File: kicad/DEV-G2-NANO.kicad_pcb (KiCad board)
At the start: 6 copper layers, 76.2 x 20.3 mm, 59 parts, among them J2 Lower Bank, J3 USB C, J3 Upper Bank, J4 HIC SWD, J5 RTC Battery, SW1 PTS815, U1 MIMXRT1171DVMAB, U10 TPS62825, U2 MAYA-W166-00B, U3 LSM6DSV, U4 LIS2MDL, U5 RTMC-G2-4IQ48, U6 W25Q64JWUUIQ, U7 MKL26Z128VFM4, U8 LM66200, U9 TPS62086, Y1 8MHz, Y2 16MHz, Y3 24MHz, Y4 32.768kHz

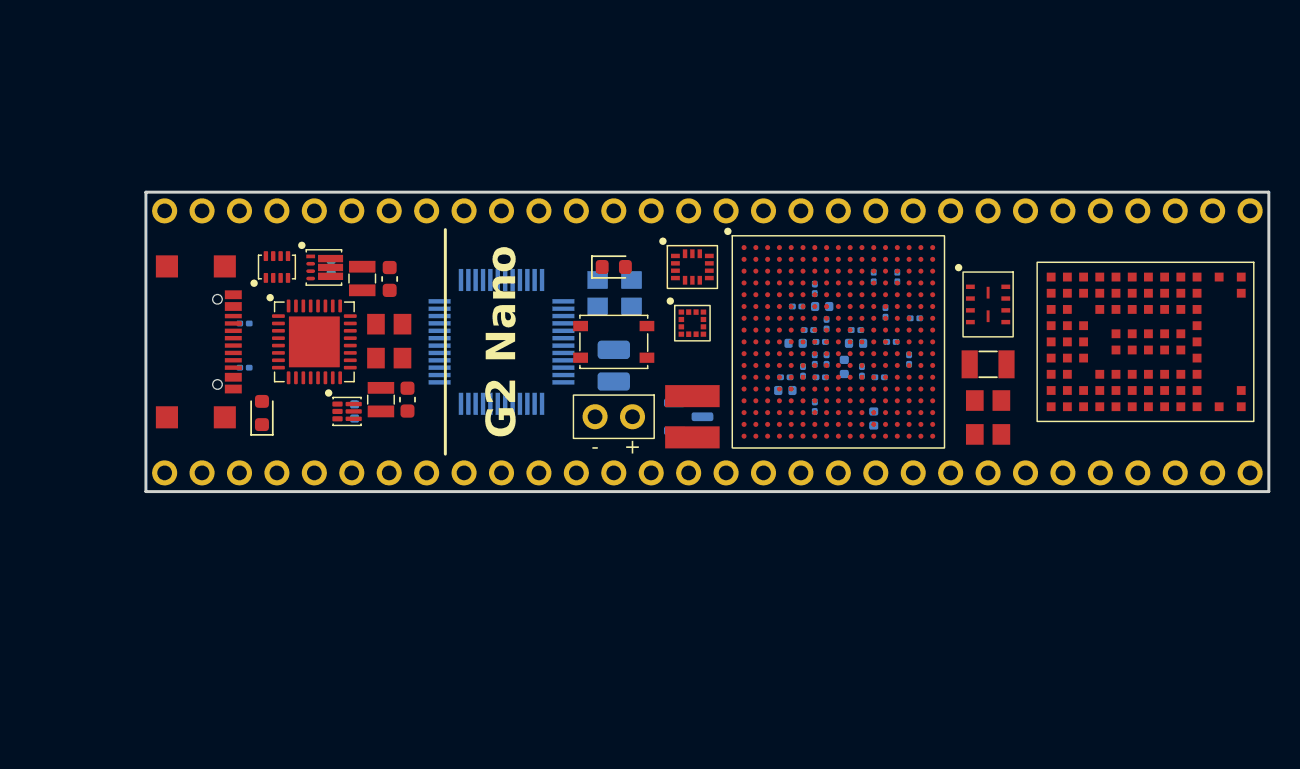
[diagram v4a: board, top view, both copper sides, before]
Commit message: finished preliminary routing
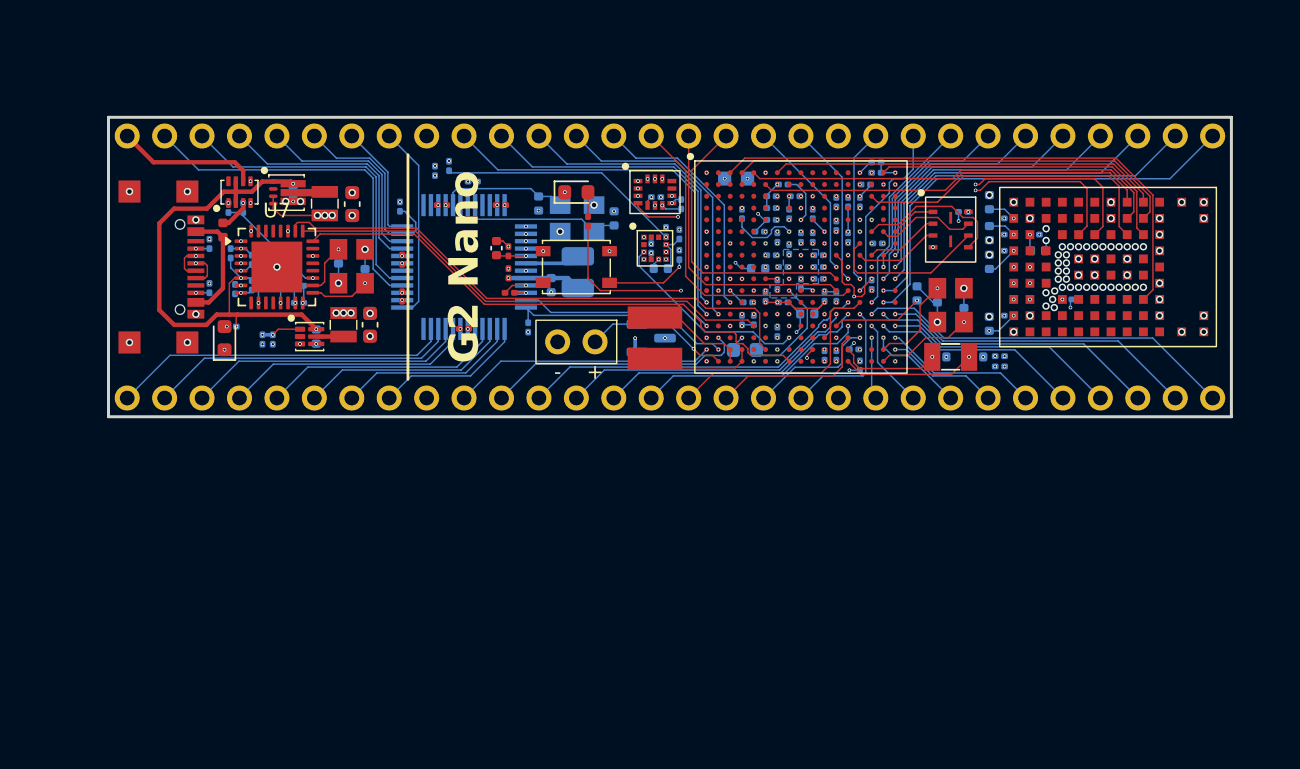
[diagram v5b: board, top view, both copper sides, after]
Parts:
- removed the C44 at (159.0, 98.5)
- removed the C47 at (166.2, 95.2)
- removed the C49 at (161.5, 92.8)
- removed the C50 at (165.4, 97.7)
- removed the C68 at (163.0, 97.0)
- removed the J3 at (190.5, 86.4)
- added C1: 100nF, Capacitor_SMD:C_0201_0603Metric, B.Cu at (174.1, 89.1)
- added C10: 10μF, Capacitor_SMD:C_0402_1005Metric, B.Cu at (172.8, 87.9)
- added C11: 100nF, Capacitor_SMD:C_0201_0603Metric, B.Cu at (151.9, 85.9)
- added C12: 100nF, Capacitor_SMD:C_0201_0603Metric, B.Cu at (150.2, 85.4)
- added C13: 100nF, Capacitor_SMD:C_0201_0603Metric, B.Cu at (151.8, 88.0)
- added C14: 100nF, Capacitor_SMD:C_0201_0603Metric, B.Cu at (150.9, 87.8)
- added C15: 10μF, Capacitor_SMD:C_0402_1005Metric, B.Cu at (150.5, 90.3)
- added C16: 220nF, Capacitor_SMD:C_0201_0603Metric, B.Cu at (149.9, 88.9)
- added C17: 10μF, Capacitor_SMD:C_0402_1005Metric, B.Cu at (143.1, 91.4)
- added C18: 100nF, Capacitor_SMD:C_0201_0603Metric, F.Cu at (140.2, 90.6)
- added C19: 100nF, Capacitor_SMD:C_0201_0603Metric, F.Cu at (140.2, 89.1)
- added C2: 100nF, Capacitor_SMD:C_0201_0603Metric, B.Cu at (174.1, 93.5)
- added C20: 10μF, Capacitor_SMD:C_0402_1005Metric, F.Cu at (139.4, 88.9)
- added C21: 100nF, Capacitor_SMD:C_0201_0603Metric, F.Cu at (139.7, 86.0)
- added C22: 100nF, Capacitor_SMD:C_0201_0603Metric, F.Cu at (140.3, 91.9)
- added C23: 100nF, Capacitor_SMD:C_0201_0603Metric, F.Cu at (135.7, 86.0)
- added C24: 100nF, Capacitor_SMD:C_0201_0603Metric, F.Cu at (133.0, 89.7)
- added C25: 100nF, Capacitor_SMD:C_0201_0603Metric, F.Cu at (133.0, 92.2)
- added C26: 100nF, Capacitor_SMD:C_0201_0603Metric, F.Cu at (137.2, 94.4)
- added C27: 15pF, Capacitor_SMD:C_0402_1005Metric, B.Cu at (142.2, 85.9)
- added C28: 15pF, Capacitor_SMD:C_0402_1005Metric, B.Cu at (147.3, 86.9)
- added C29: 100nF, Capacitor_SMD:C_0201_0603Metric, B.Cu at (122.8, 91.4)
- added C3: 100nF, Capacitor_SMD:C_0201_0603Metric, B.Cu at (174.1, 86.9)
- added C30: 2.2μF, Capacitor_SMD:C_0201_0603Metric, B.Cu at (121.3, 89.2)
- added C31: 100nF, Capacitor_SMD:C_0201_0603Metric, B.Cu at (126.0, 92.6)
- added C32: 100nF, Capacitor_SMD:C_0201_0603Metric, B.Cu at (121.6, 91.7)
- added C33: 2.2μF, Capacitor_SMD:C_0201_0603Metric, B.Cu at (126.0, 91.4)
- added C34: 100nF, Capacitor_SMD:C_0201_0603Metric, B.Cu at (171.0, 86.4)
- added C35: 15pF, Capacitor_SMD:C_0402_1005Metric, B.Cu at (130.4, 90.8)
- added C36: 15pF, Capacitor_SMD:C_0402_1005Metric, B.Cu at (128.6, 89.5)
- added C37: 2.2μF, Capacitor_SMD:C_0201_0603Metric, B.Cu at (122.8, 89.7)
- added C38: 1μF, Capacitor_SMD:C_0201_0603Metric, B.Cu at (162.4, 96.2)
- added C4: 10μF, Capacitor_SMD:C_0402_1005Metric, B.Cu at (172.8, 85.8)
- added C40: 2.2μF, Capacitor_SMD:C_0201_0603Metric, B.Cu at (156.8, 93.8)
- added C41: 22μF, Capacitor_SMD:C_0603_1608Metric, B.Cu at (155.6, 84.2)
- added C42: 2.2μF, Capacitor_SMD:C_0201_0603Metric, B.Cu at (162.4, 92.2)
- added C45: 15pF, Capacitor_SMD:C_0402_1005Metric, B.Cu at (169.3, 92.1)
- added C5: 10μF, Capacitor_SMD:C_0402_1005Metric, B.Cu at (172.8, 94.0)
- added C51: 10μF, Capacitor_SMD:C_0402_1005Metric, B.Cu at (160.4, 93.3)
- added C52: 15pF, Capacitor_SMD:C_0402_1005Metric, B.Cu at (169.4, 96.3)
- added C53: 15pF, Capacitor_SMD:C_0402_1005Metric, B.Cu at (171.9, 96.3)
- added C55: 2.2μF, Capacitor_SMD:C_0201_0603Metric, B.Cu at (160.0, 91.3)
- added C56: 22μF, Capacitor_SMD:C_0603_1608Metric, B.Cu at (156.2, 95.8)
- added C6: 10μF, Capacitor_SMD:C_0402_1005Metric, B.Cu at (172.8, 89.8)
- added C60: 2.2μF, Capacitor_SMD:C_0201_0603Metric, B.Cu at (161.2, 90.2)
- added C61: 2.2μF, Capacitor_SMD:C_0201_0603Metric, B.Cu at (161.2, 91.0)
- added C63: 100nF, Capacitor_SMD:C_0201_0603Metric, B.Cu at (161.6, 96.2)
- added C64: 2.2μF, Capacitor_SMD:C_0201_0603Metric, B.Cu at (173.5, 96.2)
- added C65: 2.2μF, Capacitor_SMD:C_0201_0603Metric, B.Cu at (173.5, 96.9)
- added C66: 4.7μF, Capacitor_SMD:C_0402_1005Metric, B.Cu at (167.9, 92.0)
- added C7: 100nF, Capacitor_SMD:C_0201_0603Metric, B.Cu at (175.9, 88.0)
- added C75: 2.2μF, Capacitor_SMD:C_0201_0603Metric, B.Cu at (158.4, 88.2)
- added C78: 1μF, Capacitor_SMD:C_0201_0603Metric, B.Cu at (124.2, 95.1)
- added C8: 100nF, Capacitor_SMD:C_0201_0603Metric, B.Cu at (174.1, 88.0)
- added C9: 10μF, Capacitor_SMD:C_0402_1005Metric, B.Cu at (176.1, 89.1)
- added FB1: 120Ω, Inductor_SMD:L_0402_1005Metric, F.Cu at (120.8, 87.7)
- added J1: Lower Bank, project_footprints:Header-1x30, B.Cu at (114.3, 99.1)
- added R1: 10kΩ, Resistor_SMD:R_0201_0603Metric, B.Cu at (151.8, 89.3)
- added R10: 10kΩ, Resistor_SMD:R_0201_0603Metric, B.Cu at (165.1, 83.8)
- added R11: 10kΩ, Resistor_SMD:R_0201_0603Metric, B.Cu at (163.2, 85.8)
- added R12: 10kΩ, Resistor_SMD:R_0201_0603Metric, B.Cu at (164.4, 84.6)
- added R14: 10kΩ, Resistor_SMD:R_0201_0603Metric, B.Cu at (121.2, 86.2)
- added R15: 10kΩ, Resistor_SMD:R_0201_0603Metric, B.Cu at (165.1, 83.1)
- added R17: 10kΩ, Resistor_SMD:R_0201_0603Metric, B.Cu at (159.2, 86.6)
- added R18: 10kΩ, Resistor_SMD:R_0201_0603Metric, B.Cu at (156.0, 86.6)
- added R19: 10kΩ, Resistor_SMD:R_0201_0603Metric, B.Cu at (158.8, 84.6)
- added R2: 2.2kΩ, Resistor_SMD:R_0201_0603Metric, F.Cu at (145.6, 87.1)
- added R20: 10kΩ, Resistor_SMD:R_0201_0603Metric, B.Cu at (158.0, 86.2)
- added R21: 10kΩ, Resistor_SMD:R_0201_0603Metric, B.Cu at (158.0, 85.4)
- added R22: 10kΩ, Resistor_SMD:R_0201_0603Metric, B.Cu at (136.1, 83.3)
- added R23: 10kΩ, Resistor_SMD:R_0201_0603Metric, B.Cu at (159.6, 85.4)
- added R24: 10kΩ, Resistor_SMD:R_0201_0603Metric, B.Cu at (135.2, 83.6)
- added R25: 10kΩ, Resistor_SMD:R_0201_0603Metric, B.Cu at (156.0, 93.8)
- added R26: 10kΩ, Resistor_SMD:R_0201_0603Metric, B.Cu at (160.0, 88.2)
- added R27: 10kΩ, Resistor_SMD:R_0201_0603Metric, B.Cu at (160.8, 88.2)
- added R28: 5.1kΩ, Resistor_SMD:R_0201_0603Metric, B.Cu at (121.4, 94.2)
- added R29: 10kΩ, Resistor_SMD:R_0201_0603Metric, B.Cu at (123.5, 95.1)
- added R3: 10kΩ, Resistor_SMD:R_0201_0603Metric, B.Cu at (178.1, 92.4)
- added R4: 10kΩ, Resistor_SMD:R_0201_0603Metric, B.Cu at (141.5, 94.3)
- added R5: 10kΩ, Resistor_SMD:R_0201_0603Metric, B.Cu at (137.8, 84.4)
- added R6: 10kΩ, Resistor_SMD:R_0201_0603Metric, B.Cu at (132.8, 86.1)
- added R7: 10kΩ, Resistor_SMD:R_0201_0603Metric, B.Cu at (160.8, 86.6)
- added R8: 10kΩ, Resistor_SMD:R_0201_0603Metric, B.Cu at (162.4, 87.4)
- added R9: 17.8kΩ, Resistor_SMD:R_0201_0603Metric, B.Cu at (122.2, 86.2)
- C46: value 4.7μF -> 15pF
- C67: value 4.7μF -> 220nF; footprint Capacitor_SMD:C_0402_1005Metric -> Capacitor_SMD:C_0201_0603Metric
- J2: value Lower Bank -> Upper Bank
- U7: footprint project_footprints:MKL26Z128VFM4 -> Package_DFN_QFN:QFN-32-1EP_5x5mm_P0.5mm_EP3.45x3.45mm
- moved J2 74.7 mm to (188.0, 81.3), turned to 90 degrees
- moved C46 9.31 mm to (171.1, 93.4)
- moved Y3 8.03 mm to (170.2, 92.7)
- moved L1 6.80 mm to (144.9, 90.5)
- moved D2 5.91 mm to (149.9, 95.0)
- moved L2 5.90 mm to (150.1, 95.0)
- moved R13 5.90 mm to (119.9, 88.6), turned to 90 degrees
- moved R16 5.90 mm to (119.9, 91.6), turned to 90 degrees
- moved C79 5.71 mm to (127.1, 94.9)
- moved C39 5.68 mm to (156.4, 92.6)
- moved C48 5.68 mm to (158.8, 92.6)
- moved C72 5.68 mm to (158.4, 94.6)
- moved C50 5.68 mm to (164.8, 91.4)
- moved C54 5.68 mm to (158.4, 91.4)
- moved C59 5.68 mm to (158.8, 90.2)
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- renumbered C43 to C39, C78 to C43, C79 to C44, C55 to C47, C56 to C48, C57 to C49, C58 to C50, C61 to C54, C64 to C57, C65 to C58, C66 to C59, C76 to C68, C77 to C69, C80 to C70, C81 to C71, C82 to C72, C83 to C73, C48 to C74, C84 to C76, C85 to C77, C87 to C79, C88 to C80
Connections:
- C43 pad 1: +1V8 -> +3V3
- C44 pad 1: +1V8 -> +3V3
- C46 pad 1: +3V3 -> GND
- C46 pad 2: GND -> Net-(U1A-XTALI)
- C62 pad 1: V_{DCDC_DIG} -> Net-(U1A-NVCC_SNVS)
- C67 pad 1: V_{DCDC_DIG} -> Net-(U1A-VDD_SNVS_DIG)
- C74 pad 1: +3V3 -> +1V8
- J2 pad 1: unconnected-(J2-Pin_1-Pad1) -> Net-(J2-Pin_1)
- J2 pad 10: unconnected-(J2-Pin_10-Pad10) -> Net-(J2-Pin_10)
- J2 pad 11: unconnected-(J2-Pin_11-Pad11) -> GND
- J2 pad 12: unconnected-(J2-Pin_12-Pad12) -> Net-(J2-Pin_12)
- J2 pad 13: unconnected-(J2-Pin_13-Pad13) -> Net-(J2-Pin_13)
- J2 pad 14: unconnected-(J2-Pin_14-Pad14) -> Net-(J2-Pin_14)
- J2 pad 15: unconnected-(J2-Pin_15-Pad15) -> Net-(J2-Pin_15)
- J2 pad 16: unconnected-(J2-Pin_16-Pad16) -> Net-(J2-Pin_16)
- J2 pad 17: unconnected-(J2-Pin_17-Pad17) -> Net-(J2-Pin_17)
- J2 pad 18: unconnected-(J2-Pin_18-Pad18) -> Net-(J2-Pin_18)
- J2 pad 19: unconnected-(J2-Pin_19-Pad19) -> Net-(J2-Pin_19)
- J2 pad 2: unconnected-(J2-Pin_2-Pad2) -> Net-(J2-Pin_2)
- J2 pad 20: unconnected-(J2-Pin_20-Pad20) -> Net-(J2-Pin_20)
- J2 pad 21: unconnected-(J2-Pin_21-Pad21) -> Net-(J2-Pin_21)
- J2 pad 22: unconnected-(J2-Pin_22-Pad22) -> +3V3
- J2 pad 23: unconnected-(J2-Pin_23-Pad23) -> UPDATE
- J2 pad 24: unconnected-(J2-Pin_24-Pad24) -> FAULT_IN
- J2 pad 25: unconnected-(J2-Pin_25-Pad25) -> FAULT_OUT
- J2 pad 26: unconnected-(J2-Pin_26-Pad26) -> M3_B
- J2 pad 27: unconnected-(J2-Pin_27-Pad27) -> M3_A
- J2 pad 28: unconnected-(J2-Pin_28-Pad28) -> E3_B
- J2 pad 29: unconnected-(J2-Pin_29-Pad29) -> E3_A
- J2 pad 3: unconnected-(J2-Pin_3-Pad3) -> Net-(J2-Pin_3)
- J2 pad 30: unconnected-(J2-Pin_30-Pad30) -> V_{IN}
- J2 pad 4: unconnected-(J2-Pin_4-Pad4) -> Net-(J2-Pin_4)
- J2 pad 5: unconnected-(J2-Pin_5-Pad5) -> Net-(J2-Pin_5)
- J2 pad 6: unconnected-(J2-Pin_6-Pad6) -> Net-(J2-Pin_6)
- J2 pad 7: unconnected-(J2-Pin_7-Pad7) -> Net-(J2-Pin_7)
- J2 pad 8: unconnected-(J2-Pin_8-Pad8) -> Net-(J2-Pin_8)
- J2 pad 9: unconnected-(J2-Pin_9-Pad9) -> Net-(J2-Pin_9)
- SW1 pad 2: Net-(R1-Pad1) -> Net-(U1C-GPIO_EMC_B1_38)
- U1 pad A16: (no net) -> Net-(U1C-GPIO_SD_B1_05)
- U1 pad A3: (no net) -> Net-(U1C-GPIO_EMC_B1_09)
- U1 pad A4: (no net) -> Net-(U1C-GPIO_DISP_B2_15)
- U1 pad A7: (no net) -> Net-(U1C-GPIO_DISP_B2_14)
- U1 pad B16: (no net) -> Net-(U1C-GPIO_SD_B1_00)
- U1 pad B17: (no net) -> Net-(U1C-GPIO_SD_B1_03)
- U1 pad C15: (no net) -> Net-(U1C-GPIO_SD_B1_02)
- U1 pad F1: (no net) -> Net-(U1C-GPIO_EMC_B1_35)
- U1 pad F6: +3V3 -> +1V8
- U1 pad F7: +3V3 -> +1V8
- U1 pad G1: (no net) -> Net-(U1C-GPIO_EMC_B1_36)
- U1 pad G12: Net-(U1A-VDD_USB_3P3) -> +3V3
- U1 pad G6: +3V3 -> +1V8
- U1 pad H12: Net-(U1A-VDD_USB_1P8) -> V_{DCDC_ANA}
- U1 pad H17: (no net) -> Net-(J2-Pin_5)
- U1 pad H6: +1V8 -> +3V3
- U1 pad J1: (no net) -> Net-(U1C-GPIO_EMC_B1_38)
- U1 pad J12: (no net) -> Net-(J2-Pin_13)
- U1 pad J16: (no net) -> Net-(J2-Pin_7)
- U1 pad J17: (no net) -> Net-(J2-Pin_4)
- U1 pad J6: +1V8 -> +3V3
- U1 pad K12: (no net) -> Net-(J2-Pin_14)
- U1 pad K13: (no net) -> Net-(J2-Pin_12)
- U1 pad K14: (no net) -> Net-(J2-Pin_10)
- U1 pad K16: (no net) -> Net-(J2-Pin_6)
- U1 pad K17: (no net) -> Net-(J2-Pin_3)
- U1 pad K2: (no net) -> Net-(U1C-GPIO_EMC_B2_00)
- U1 pad K3: (no net) -> Net-(U1C-GPIO_EMC_B2_02)
- U1 pad K4: (no net) -> Net-(U1C-GPIO_EMC_B2_01)
- U1 pad L12: (no net) -> Net-(J2-Pin_15)
- U1 pad L13: (no net) -> Net-(J2-Pin_16)
- U1 pad L14: (no net) -> Net-(J2-Pin_9)
- U1 pad L16: (no net) -> Net-(J2-Pin_2)
- U1 pad L2: (no net) -> Net-(U1C-GPIO_EMC_B2_15)
- U1 pad M1: (no net) -> Net-(J2-Pin_19)
- U1 pad M13: (no net) -> Net-(J1-Pin_12)
- U1 pad M14: (no net) -> Net-(J1-Pin_16)
- U1 pad M15: (no net) -> Net-(J2-Pin_8)
- U1 pad M16: (no net) -> Net-(J2-Pin_1)
- U1 pad M3: (no net) -> Net-(J2-Pin_17)
- U1 pad N1: (no net) -> Net-(J2-Pin_20)
- U1 pad N12: (no net) -> Net-(J1-Pin_13)
- U1 pad N13: (no net) -> Net-(J1-Pin_14)
- U1 pad N14: (no net) -> Net-(J1-Pin_19)
- U1 pad N15: (no net) -> Net-(J1-Pin_30)
- U1 pad N16: (no net) -> Net-(J1-Pin_28)
- U1 pad N17: (no net) -> Net-(J1-Pin_29)
- U1 pad N2: (no net) -> Net-(J2-Pin_18)
- U1 pad N7: (no net) -> Net-(U1C-GPIO_LPSR_04)
- U1 pad N8: (no net) -> Net-(U1C-GPIO_LPSR_05)
- U1 pad P1: (no net) -> Net-(J2-Pin_21)
- U1 pad P13: (no net) -> Net-(J1-Pin_15)
- U1 pad P15: (no net) -> Net-(J1-Pin_22)
- U1 pad P16: (no net) -> Net-(J1-Pin_26)
- U1 pad P17: (no net) -> Net-(J1-Pin_27)
- U1 pad P8: (no net) -> Net-(U1C-GPIO_LPSR_06)
- U1 pad R1: (no net) -> Net-(U1C-GPIO_EMC_B2_03)
- U1 pad R13: (no net) -> Net-(J1-Pin_17)
- U1 pad R14: (no net) -> Net-(J1-Pin_18)
- U1 pad R15: (no net) -> Net-(J1-Pin_21)
- U1 pad R16: (no net) -> Net-(J1-Pin_23)
- U1 pad R17: (no net) -> Net-(J1-Pin_25)
- U1 pad R2: (no net) -> Net-(J1-Pin_11)
- U1 pad R8: (no net) -> Net-(U1C-GPIO_LPSR_07)
- U1 pad T1: (no net) -> Net-(J1-Pin_10)
- U1 pad T17: (no net) -> Net-(J1-Pin_24)
- U1 pad T2: (no net) -> Net-(U1C-GPIO_EMC_B2_17)
- U1 pad U2: (no net) -> Net-(U1C-GPIO_EMC_B2_19)
- U1 pad U5: (no net) -> Net-(U1C-GPIO_LPSR_12)
- U2 pad E7: Net-(U2A-BT_WAKE_HOST) -> Net-(U1C-GPIO_SD_B1_00)
- U2 pad F7: Net-(U2A-WLAN_WAKE_HOST) -> Net-(U1C-GPIO_SD_B1_03)
- U2 pad H7: Net-(U2A-WLAN_RESET) -> Net-(U1C-GPIO_SD_B1_02)
- U2 pad J3: Net-(U2A-PDn) -> Net-(U1C-GPIO_EMC_B1_09)
- U2 pad J7: Net-(U2A-BT_RESET) -> Net-(U1C-GPIO_SD_B1_05)
- U2 pad J8: Net-(U2A-WLAN_DEV_WAKE) -> Net-(U1C-GPIO_DISP_B2_15)
- U2 pad J9: Net-(U2A-BT_DEV_WAKE) -> Net-(U1C-GPIO_DISP_B2_14)
- U3 pad 1: Net-(U3-SDO) -> Net-(U1C-GPIO_LPSR_05)
- U3 pad 12: Net-(U3-CS) -> Net-(U1C-GPIO_LPSR_06)
- U3 pad 13: Net-(U3-SCL) -> Net-(U1C-GPIO_LPSR_12)
- U3 pad 14: Net-(U3-SDI) -> Net-(U1C-GPIO_LPSR_04)
- U3 pad 4: Net-(U3-INT1) -> Net-(U1C-GPIO_EMC_B1_36)
- U3 pad 9: Net-(U3-INT2) -> Net-(U1C-GPIO_EMC_B1_35)
- U4 pad 1: Net-(U3-SCL) -> Net-(U1C-GPIO_LPSR_12)
- U4 pad 3: Net-(U4-CS) -> Net-(U1C-GPIO_LPSR_07)
- U4 pad 4: Net-(U3-SDI) -> Net-(U1C-GPIO_LPSR_04)
- U4 pad 7: Net-(U3-SDO) -> Net-(U1C-GPIO_LPSR_05)
- U5 pad 37: Net-(U5-CS_N) -> Net-(U1C-GPIO_EMC_B2_01)
- U5 pad 38: Net-(U5-SCLK) -> Net-(U1C-GPIO_EMC_B2_00)
- U5 pad 39: Net-(U5-DI) -> Net-(U1C-GPIO_EMC_B2_02)
- U5 pad 40: Net-(U5-DO) -> Net-(U1C-GPIO_EMC_B2_03)
- U5 pad 47: Net-(U5-INTER) -> Net-(U1C-GPIO_EMC_B2_17)
- U5 pad 48: Net-(U5-RESET_N) -> Net-(U1C-GPIO_EMC_B2_19)
- U7 pad 1: (no net) -> Net-(U1B-GPIO_LPSR_03)
- U7 pad 32: (no net) -> Net-(U1B-GPIO_LPSR_02)
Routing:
- net +1V8: track 0.00 -> 90.2 mm, vias 0 -> 26
- net Net-(U1B-GPIO_LPSR_03): track 0.00 -> 52.5 mm, vias 0 -> 3
- net Net-(U1B-GPIO_LPSR_02): track 0.00 -> 49.2 mm, vias 0 -> 3
- net RC_DELAY: track 0.00 -> 45.0 mm, vias 0 -> 3
- net Net-(U1B-POR_B): track 0.00 -> 39.2 mm, vias 0 -> 2
- net GND: track 0.00 -> 38.8 mm, vias 0 -> 173
- net Net-(U1C-GPIO_EMC_B1_09): track 0.00 -> 37.5 mm
- net Net-(U1B-GPIO_LPSR_15): track 0.00 -> 37.2 mm, vias 0 -> 2
- net Net-(U1B-GPIO_LPSR_14): track 0.00 -> 37.2 mm
- net Net-(U1B-GPIO_LPSR_08): track 0.00 -> 36.7 mm
- net +5V: track 0.00 -> 35.7 mm, vias 0 -> 4
- net Net-(U1B-GPIO_LPSR_09): track 0.00 -> 33.3 mm
- net Net-(U1C-GPIO_DISP_B2_15): track 0.00 -> 30.7 mm
- net Net-(J2-Pin_1): track 0.00 -> 30.1 mm, vias 0 -> 1
- net Net-(U1C-GPIO_DISP_B2_13): track 0.00 -> 28.8 mm
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- added copper zone on In4.Cu, net +1V8
- added copper zone on In4.Cu, net +3V3
- added copper zone on In1.Cu, net GND
- added copper zone on In3.Cu, net GND
- added copper zone on B.Cu, net V_{DCDC_DIG}
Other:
- board text added: "+3V3"
- board text added: "AD_00"
- board text added: "AD_01"
- board text added: "AD_02"
- board text added: "AD_03"
- board text added: "AD_04"
- board text added: "AD_05"
- board text added: "AD_06"
- board text added: "AD_07"
- board text added: "AD_08"
- board text added: "AD_09"
- board text added: "AD_10"
- board text added: "AD_11"
- board text added: "AD_12"
- board text added: "AD_13"
- board text added: "AD_14"
- board text added: "AD_15"
- board text added: "AD_16"
- board text added: "AD_17"
- board text added: "AD_18"
- board text added: "AD_19"
- board text added: "AD_20"
- board text added: "AD_21"
- board text added: "AD_22"
- board text added: "AD_23"
- board text added: "AD_24"
- board text added: "AD_25"
- board text added: "AD_26"
- board text added: "AD_27"
- board text added: "AD_30"
- board text added: "AD_31"
- board text added: "AD_32"
- board text added: "AD_33"
- board text added: "AD_34"
- board text added: "E1_A"
- board text added: "E1_B"
- board text added: "E2_A"
- board text added: "E2_B"
- board text added: "E3_A"
- board text added: "E3_B"
- board text added: "EMC_B2_04"
- board text added: "EMC_B2_05"
- board text added: "EMC_B2_06"
- board text added: "EMC_B2_07"
- board text added: "EMC_B2_08"
- board text added: "EMC_B2_09"
- board text added: "EMC_B2_10"
- board text added: "FAULT_IN"
- board text added: "FAULT_OUT"
- board text added: "M1_A"
- board text added: "M1_B"
- board text added: "M2_A"
- board text added: "M2_B"
- board text added: "M3_A"
- board text added: "M3_B"
- board text added: "UPDATE"

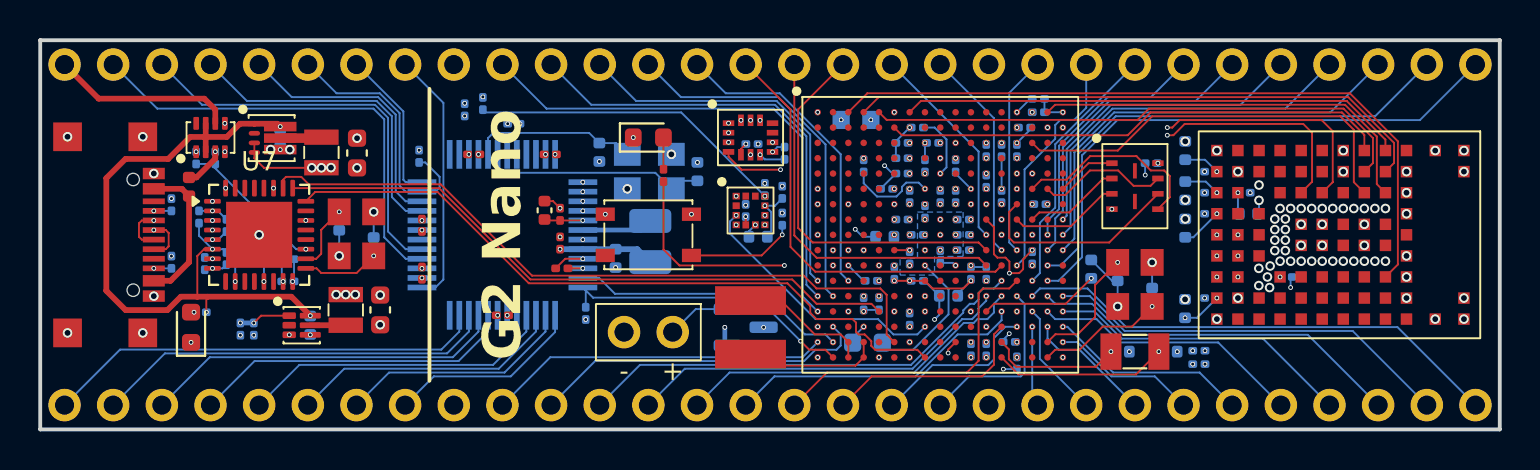
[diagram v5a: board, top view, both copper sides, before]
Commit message: added stitching vias and made cosmetic changes
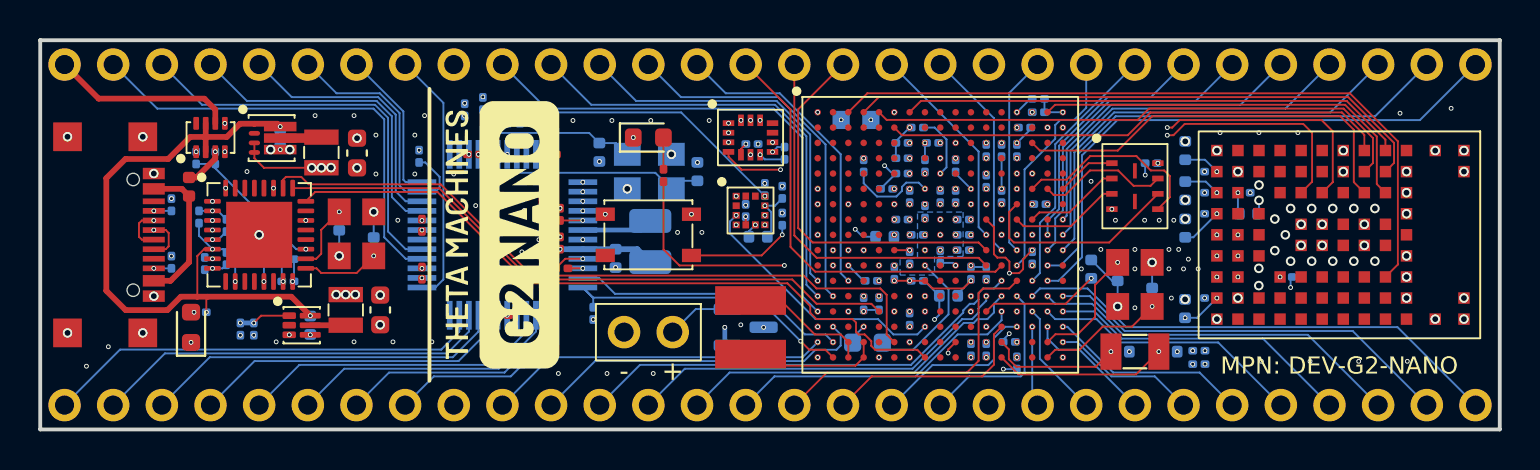
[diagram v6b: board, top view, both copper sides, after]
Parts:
- added G***: LOGO, LOGO, F.Cu at (137.2, 90.2)
- U7: footprint Package_DFN_QFN:QFN-32-1EP_5x5mm_P0.5mm_EP3.45x3.45mm -> project_footprints:MKL26Z128VFM4
- moved R4 0.39 mm to (141.9, 94.3)
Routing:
- net +1V8: track 90.2 -> 89.2 mm
- net GND: vias 173 -> 215
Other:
- board text added: "MPN: DEV-G2-NANO"
- board text removed: "G2 Nano"
